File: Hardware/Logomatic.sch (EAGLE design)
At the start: 71 parts, among them J1 USD_CONNECTOR, Q1 12MHz, Q2 32kHz, Q4 TRANSISTOR_PNPSMD, U1 MCP73831, U2 3.3V, U4 LPC213X, X1 USB_MICROB_PLUGCONN-11752

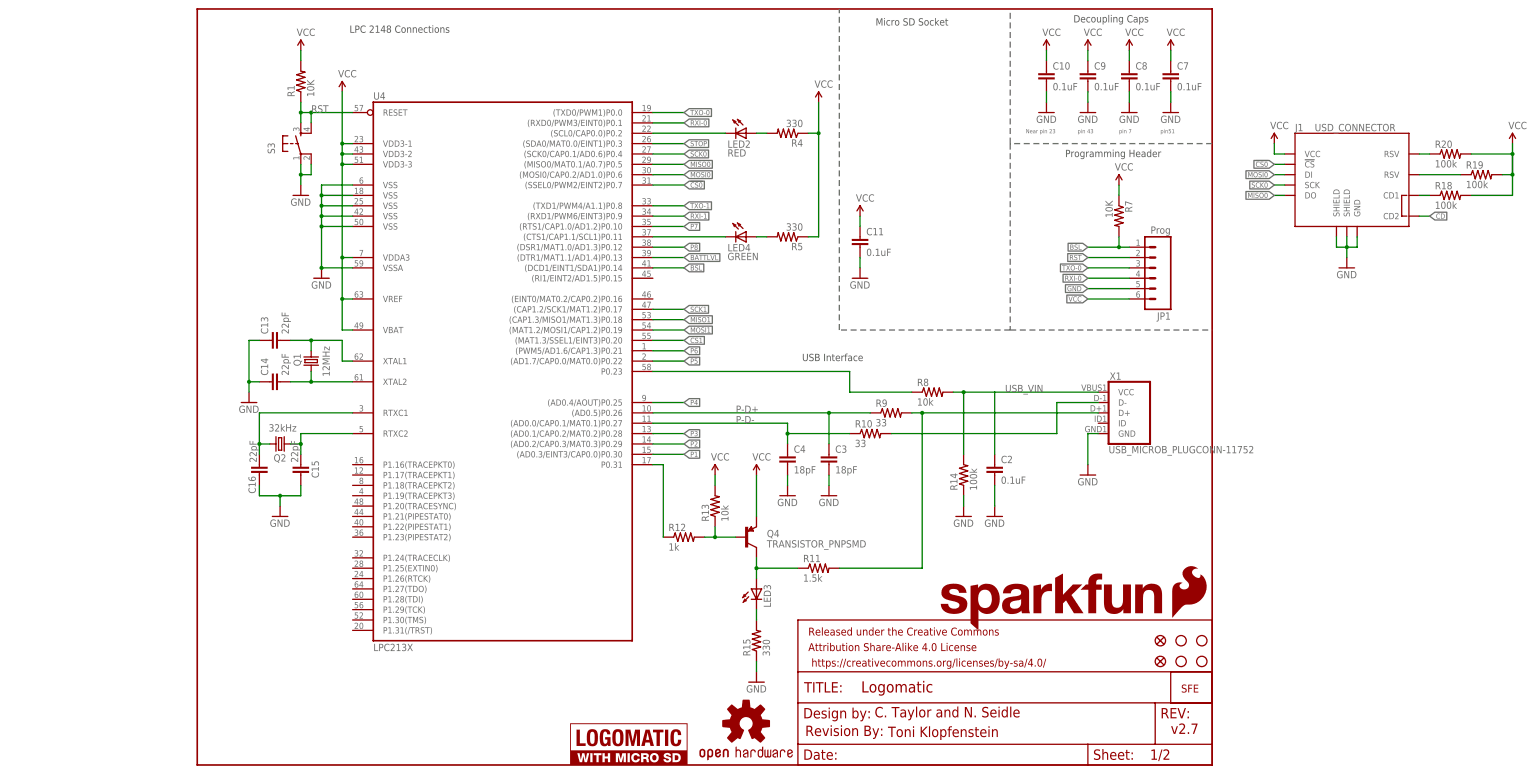
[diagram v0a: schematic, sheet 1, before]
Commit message: Added coin cell holder
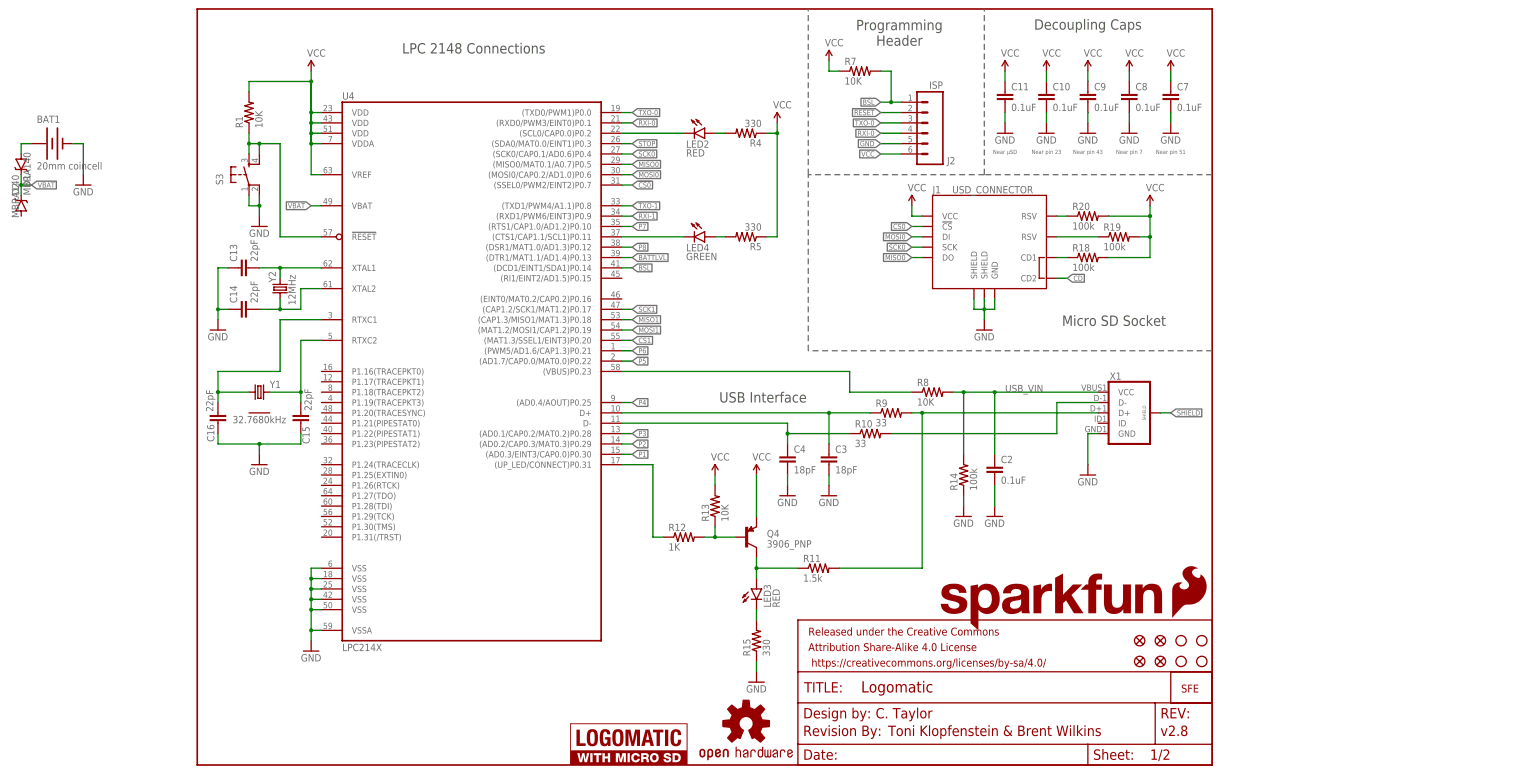
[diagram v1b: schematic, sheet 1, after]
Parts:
- removed JP1: Prog, SparkFun:M06SIP
- removed JP2: LiPo, SparkFun:M02-JST-2MM-SMT
- removed JP4: (no value), SparkFun:M04PTH
- removed JP5: (no value), SparkFun:M06SIP
- removed JP6: M100.1, SparkFun:M10"
- removed Q1: 12MHz, SparkFunEagle-6-6-07:CRYSTAL5X3
- removed Q2: 32kHz, SparkFun:CRYSTAL32-SMD
- removed U$1, U$2: FIDUCIAL1X2, SparkFun:FIDUCIAL1X2
- removed U$3, U$4, U$5, U$8: STAND-OFF, SparkFun:STAND-OFF
- added BAT1: 20mm coincell, SparkFun-Electromechanical:BATTERY20MM_4LEGS
- added D1, D2: MBRA140, SparkFun-DiscreteSemi:MBRA140
- added FD1, FD2, FD3, FD4: FIDUCIAL1X2, SparkFun-Aesthetics:FIDUCIAL1X2
- added H1, H2, H3, H4: STAND-OFF, SparkFun-Electromechanical:STAND-OFF
- added J2: ISP, SparkFun-Connectors:M06SILK_FEMALE_PTH
- added J3: LiPo, SparkFun-Connectors:M02-JST-2MM-SMT
- added J4: (no value), SparkFun-Connectors:M04PTH
- added J5: (no value), SparkFun-Connectors:M06SILK_FEMALE_PTH
- added J6: M100.1, SparkFun-Connectors:M10SILK_FEMALE_PTH
- added Y1: 32.7680kHz, Logomatic_testing:RTC_CRYSTAL32-SMD
- added Y2: 12MHz, SparkFun-FreqCtrl:CRYSTALCRYSTAL-SMD-5X3-12MHZ
- FRAME4: value FRAME-LETTER -> FRAME-LETTERNO_PACKAGE; device SparkFun-Aesthetics:FRAME-LETTER -> SparkFun-Aesthetics:FRAME-LETTERNO_PACKAGE
- LED1: value LED RED -> RED
- LED3: value (none) -> RED
- Q4: value TRANSISTOR_PNPSMD -> 3906_PNP; device SparkFun:TRANSISTOR_PNPSMD -> SparkFun-DiscreteSemi:TRANSISTOR_PNPPMBT3906
- R1, R6, R7: device SparkFun-Resistors:10KOHM1/10W1%(0603)0603 -> SparkFun-Resistors:10KOHM-1/10W-1%(0603)0603
- R12: value 1k -> 1K; device SparkFun-Resistors:1KOHM1/10W1%(0603) -> SparkFun-Resistors:1KOHM-1/10W-1%(0603)
- R13, R8: value 10k -> 10K; device SparkFun-Resistors:10KOHM1/10W1%(0603)0603 -> SparkFun-Resistors:10KOHM-1/10W-1%(0603)0603
- R14: device SparkFun-Resistors:100KOHM1/10W1%(0603) -> SparkFun-Resistors:100KOHM-1/10W-1%(0603)
- R16, R17: value 1M -> DNP; device SparkFun-Resistors:1MOHM1/10W1%(0603) -> SparkFun-Resistors:1MOHM-1/10W-1%(0603)
- S1: device SparkFun:SWITCH-SPSTSMD -> SparkFun-Electromechanical:SWITCH-SPDTSMD
- S2: value Stop -> TAC_SWITCHSMD; device SparkFunEagle-6-6-07:TAC_SWITCHSND -> SparkFun-Retired:TAC_SWITCHSMD
- S3: value Reset -> RESET; device SparkFunEagle-6-6-07:TAC_SWITCHSND -> SparkFun-Retired:TAC_SWITCHSMD
- U1: device SparkFun:MCP73831SMD -> SparkFun-PowerIC:MCP73831
- U2: device SparkFun:V_REG_LDOSMD -> SparkFun-PowerIC:MIC52053.3V
- U4: value LPC213X -> LPC214X; device SparkFun:LPC213X -> SparkFun-DigitalIC:LPC214X
- X1: value USB_MICROB_PLUGCONN-11752 -> (none)
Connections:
- removed net N$16: R8.1, U4.P0.23
- removed net N$21: C14.2, Q1.1, U4.XTAL2
- removed net N$31: R12.1, U4.P0.31
- removed net N$5: C13.2, Q1.2, U4.XTAL1
- removed net N$6: C16.2, Q2.2, U4.RTXC1
- removed net N$9: C15.2, Q2.1, U4.RTXC2
- removed net RST: JP1.2, R1.1, S3.3, S3.4, U4.RESET
- new net !RESET: J2.2, R1.1, S3.3, S3.4, U4.!RESET
- new net N$2: BAT1.+, D1.A
- new net RTXC1: C16.2, U4.RTXC1, Y1.1
- new net RTXC2: C15.2, U4.RTXC2, Y1.4
- new net SHIELD: X1.SHIELD
- new net UP_LED: R12.1, U4.(UP_LED/CONNECT)P0.31
- new net VBAT: D1.C, D2.C, U4.VBAT
- new net VBUS: R8.1, U4.(VBUS)P0.23
- new net XTAL1: C13.2, U4.XTAL1, Y2.2
- new net XTAL2: C14.2, U4.XTAL2, Y2.1
- net BSL: now also J2.1; no longer JP1.1
- net CS1: now also J4.1; no longer JP4.1
- net GND: now also BAT1.-, J2.5, J3.2, J5.4, J6.10, U4.VSS@5; no longer JP1.5, JP2.1, JP5.4, JP6.10, U4.VSS
- net MISO1: now also J4.3; no longer JP4.3
- net MOSI1: now also J4.2; no longer JP4.2
- net P-D+: now also U4.D+; no longer U4.(AD0.5)P0.26
- net P-D-: now also U4.D-; no longer U4.(AD0.0/CAP0.1/MAT0.1)P0.27
- net P1: now also J6.2; no longer JP6.2
- net P2: now also J6.3; no longer JP6.3
- net P3: now also J6.4; no longer JP6.4
- net P4: now also J6.5; no longer JP6.5
- net P5: now also J6.6; no longer JP6.6
- net P6: now also J6.7; no longer JP6.7
- net P7: now also J6.8; no longer JP6.8
- net P8: now also J6.9; no longer JP6.9
- net RAW: now also J5.1; no longer JP5.1
- net RXI-0: now also J2.4; no longer JP1.4
- net RXI-1: now also J5.6; no longer JP5.6
- net SCK1: now also J4.4; no longer JP4.4
- net STOP: now also J6.1; no longer JP6.1
- net TXO-0: now also J2.3; no longer JP1.3
- net TXO-1: now also J5.5; no longer JP5.5
- net USB_VIN: now also J5.2; no longer JP5.2
- net VCC: now also J2.6, J5.3, U4.VDD@1, U4.VDD@2, U4.VDD@3, U4.VDDA; no longer JP1.6, JP5.3, U4.VBAT, U4.VDD3-1, U4.VDD3-2, U4.VDD3-3, U4.VDDA3
- net VLIPO: now also J3.1; no longer JP2.2
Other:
- note added: "C. Taylor"
- note added: "Near pin 43"
- note added: "Near pin 51"
- note added: "Near pin 7"
- note added: "Near µSD"
- note added: "Plated Through Holes"
- note added: "Toni Klopfenstein & Brent Wilkins"
- note added: "v2.8"
- note removed: "Breakouts"
- note removed: "C. Taylor and N. Seidle"
- note removed: "Toni Klopfenstein"
- note removed: "pin 43"
- note removed: "pin 7"
- note removed: "pin51"
- note removed: "v2.7"
- moved on the sheet: C10, C11, C13, C14, C15, C16, C7, C8, C9, J1, R1, R18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

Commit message: Tweaks
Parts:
- removed LOGO3: SFE_LOGO_FLAME.4_INCH, SparkFun-Aesthetics:SFE_LOGO_FLAME.4_INCH
- removed U$10: REVISION, SparkFun-Aesthetics:REVISION
- removed U$7: LOGO-SFESK, SparkFun:LOGO-SFESK
- added LOGO5: SFE_LOGO_FLAME.1_INCH, SparkFun-Aesthetics:SFE_LOGO_FLAME.1_INCH
- R11: value 1.5k -> 1.5KOHM; device SparkFun-Resistors:1.5KOHM1/10W1%(0603) -> SparkFun-Resistors:1.5KOHM-1/10W-1%(0603)
- S1: value (none) -> BATTERY_POWER
- X1: value (none) -> Micro-B
- renumbered U$6 to LOGO4
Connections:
- net VCC: now also D2.A
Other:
- note added: "Charge Circuit (1S)"
- note added: "Limit RAW voltage to 6.5V"
- note added: "RTC Battery Backup"
- note removed: "C. Taylor"
- note removed: "Charge Circuit"
- note removed: "Toni Klopfenstein & Brent Wilkins"
- note removed: "v2.8"
- moved on the sheet: C1, C17, C5, J1, J2, J3, J4, J5, J6, LED1, R1, R18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

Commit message: Fixed issue #9 on GitHub
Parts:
- removed FRAME4: FRAME-LETTERNO_PACKAGE, SparkFun-Aesthetics:FRAME-LETTERNO_PACKAGE
- removed LOGO5: SFE_LOGO_FLAME.1_INCH, SparkFun-Aesthetics:SFE_LOGO_FLAME.1_INCH
- removed U4: LPC214X, SparkFun-DigitalIC:LPC214X
- added FRAME1: FRAME-LETTER, SparkFun-Aesthetics:FRAME-LETTER
- added LOGO100: OSHW-LOGOL, SparkFun-Aesthetics:OSHW-LOGOL
- added U3: 3.3V, SparkFun-PowerIC:MIC52053.3V
- C1: value 0.1uF -> 4.7uF; device SparkFun-Capacitors:0.1UF-25V(+80/-20%)(0603) -> SparkFun-Capacitors:4.7UF-6.3V-10%(0603)0603
- C10: value 0.1uF -> 10uF; device SparkFun-Capacitors:0.1UF-25V(+80/-20%)(0603) -> SparkFun-Capacitors:10UF-16V-10%(TANT)
- C12: value 0.1uF -> 22pF; device SparkFun-Capacitors:0.1UF-25V(+80/-20%)(0603) -> SparkFun-Capacitors:22PF-50V-5%(0603)
- C14, C15: value 22pF -> 0.1uF; device SparkFun-Capacitors:22PF-50V-5%(0603) -> SparkFun-Capacitors:0.1UF-25V(+80/-20%)(0603)
- C16: value 22pF -> 18pF; device SparkFun-Capacitors:22PF-50V-5%(0603) -> SparkFun-Capacitors:18PF-50V-5%(0603)
- C17: value 4.7uF -> 0.1uF; device SparkFun-Capacitors:4.7UF-6.3V-10%(0603)0603 -> SparkFun-Capacitors:0.1UF-25V(+80/-20%)(0603)
- C3: value 18pF -> 0.1uF; device SparkFun-Capacitors:18PF-50V-5%(0603) -> SparkFun-Capacitors:0.1UF-25V(+80/-20%)(0603)
- C4: value 18pF -> 4.7uF; device SparkFun-Capacitors:18PF-50V-5%(0603) -> SparkFun-Capacitors:4.7UF-6.3V-10%(0603)0603
- C5: value 4.7uF -> 22pF; device SparkFun-Capacitors:4.7UF-6.3V-10%(0603)0603 -> SparkFun-Capacitors:22PF-50V-5%(0603)
- C6: value 10uF -> 22pF; device SparkFun-Capacitors:10UF-16V-10%(TANT) -> SparkFun-Capacitors:22PF-50V-5%(0603)
- C9: value 0.1uF -> 18pF; device SparkFun-Capacitors:0.1UF-25V(+80/-20%)(0603) -> SparkFun-Capacitors:18PF-50V-5%(0603)
- FRAME2: value FRAME-LETTER -> FRAME-LETTERNO_PACKAGE; device SparkFun-Aesthetics:FRAME-LETTER -> SparkFun-Aesthetics:FRAME-LETTERNO_PACKAGE
- J1: value USD_CONNECTOR -> ISP; device SparkFun-Connectors:USD_CONNECTOR -> SparkFun-Connectors:M06SILK_FEMALE_PTH
- J2: value ISP -> LiPo; device SparkFun-Connectors:M06SILK_FEMALE_PTH -> SparkFun-Connectors:M02-JST-2MM-SMT
- J3: value LiPo -> USD_CONNECTOR; device SparkFun-Connectors:M02-JST-2MM-SMT -> SparkFun-Connectors:USD_CONNECTOR
- J5: value (none) -> M100.1; device SparkFun-Connectors:M06SILK_FEMALE_PTH -> SparkFun-Connectors:M10SILK_FEMALE_PTH
- J6: value M100.1 -> (none); device SparkFun-Connectors:M10SILK_FEMALE_PTH -> SparkFun-Connectors:M06SILK_FEMALE_PTH
- LED2: value RED -> GREEN; device SparkFun-LED:LED-RED0603 -> SparkFun-LED:LED-GREEN0603
- LED4: value GREEN -> RED; device SparkFun-LED:LED-GREEN0603 -> SparkFun-LED:LED-RED0603
- LOGO1: value OSHW-LOGOL -> SFE_LOGO_NAME.1_INCH; device SparkFun-Aesthetics:OSHW-LOGOL -> SparkFun-Aesthetics:SFE_LOGO_NAME.1_INCH
- LOGO2: value SFE_LOGO_NAME.1_INCH -> SFE_LOGO_FLAME.1_INCH; device SparkFun-Aesthetics:SFE_LOGO_NAME.1_INCH -> SparkFun-Aesthetics:SFE_LOGO_FLAME.1_INCH
- R10: value 33 -> 10K; device SparkFun-Resistors:33OHM1/10W1%(0603) -> SparkFun-Resistors:10KOHM-1/10W-1%(0603)0603
- R11: value 1.5KOHM -> 10K; device SparkFun-Resistors:1.5KOHM-1/10W-1%(0603) -> SparkFun-Resistors:10KOHM-1/10W-1%(0603)0603
- R12: value 1K -> 1.5KOHM; device SparkFun-Resistors:1KOHM-1/10W-1%(0603) -> SparkFun-Resistors:1.5KOHM-1/10W-1%(0603)
- R13: value 10K -> 1K; device SparkFun-Resistors:10KOHM-1/10W-1%(0603)0603 -> SparkFun-Resistors:1KOHM-1/10W-1%(0603)
- R14: value 100k -> 10K; device SparkFun-Resistors:100KOHM-1/10W-1%(0603) -> SparkFun-Resistors:10KOHM-1/10W-1%(0603)0603
- R15: value 330 -> 33; device SparkFun-Resistors:330OHM1/10W1%(0603) -> SparkFun-Resistors:33OHM1/10W1%(0603)
- R16: value DNP -> 33; device SparkFun-Resistors:1MOHM-1/10W-1%(0603) -> SparkFun-Resistors:33OHM1/10W1%(0603)
- R17: value DNP -> 100k; device SparkFun-Resistors:1MOHM-1/10W-1%(0603) -> SparkFun-Resistors:100KOHM-1/10W-1%(0603)
- R2: value 2.0k -> 10K; device SparkFun-Resistors:2.0KOHM1/10W5%(0603) -> SparkFun-Resistors:10KOHM-1/10W-1%(0603)0603
- R5: value 330 -> 2.0k; device SparkFun-Resistors:330OHM1/10W1%(0603) -> SparkFun-Resistors:2.0KOHM1/10W5%(0603)
- R6, R7: value 10K -> DNP; device SparkFun-Resistors:10KOHM-1/10W-1%(0603)0603 -> SparkFun-Resistors:1MOHM-1/10W-1%(0603)
- R8: value 10K -> 330; device SparkFun-Resistors:10KOHM-1/10W-1%(0603)0603 -> SparkFun-Resistors:330OHM1/10W1%(0603)
- R9: value 33 -> 330; device SparkFun-Resistors:33OHM1/10W1%(0603) -> SparkFun-Resistors:330OHM1/10W1%(0603)
- S1: value BATTERY_POWER -> RESET; device SparkFun-Electromechanical:SWITCH-SPDTSMD -> SparkFun-Retired:TAC_SWITCHSMD
- S2: value TAC_SWITCHSMD -> BATTERY_POWER; device SparkFun-Retired:TAC_SWITCHSMD -> SparkFun-Electromechanical:SWITCH-SPDTSMD
- S3: value RESET -> TAC_SWITCHSMD
- U2: value 3.3V -> LPC214X; device SparkFun-PowerIC:MIC52053.3V -> SparkFun-DigitalIC:LPC214X
- Y1: value 32.7680kHz -> 12MHz; device Logomatic_testing:RTC_CRYSTAL32-SMD -> SparkFun-FreqCtrl:CRYSTALCRYSTAL-SMD-5X3-12MHZ
- Y2: value 12MHz -> 32.7680kHz; device SparkFun-FreqCtrl:CRYSTALCRYSTAL-SMD-5X3-12MHZ -> Logomatic_testing:RTC_CRYSTAL32-SMD
- renumbered BAT1 to BAT100, D1 to D101, D2 to D100, FD3 to FD100, FD4 to FD101, LOGO4 to LOGO101, Q4 to Q1, R18 to R101, R19 to R100, R20 to R102
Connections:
- net !CS0: now also J3.!CS, U2.(SSEL0/PWM2/EINT2)P0.7; no longer J1.!CS, U4.(SSEL0/PWM2/EINT2)P0.7
- net !RESET: now also J1.2, S1.3, S1.4, U2.!RESET; no longer J2.2, S3.3, S3.4, U4.!RESET
- net BATTLVL: now also R6.1, R7.2, U2.(DTR1/MAT1.1/AD1.4)P0.13; no longer R16.2, R17.1, U4.(DTR1/MAT1.1/AD1.4)P0.13
- net BSL: now also J1.1, R2.2, U2.(DCD1/EINT1/SDA1)P0.14; no longer J2.1, R7.2, U4.(DCD1/EINT1/SDA1)P0.14
- net CD: now also J3.CD2; no longer J1.CD2
- net CS1: now also U2.(MAT1.3/SSEL1/EINT3)P0.20; no longer U4.(MAT1.3/SSEL1/EINT3)P0.20
- net GND: now also C10.-, C12.1, C14.2, C15.2, C16.2, C5.1, C6.1, J1.5, J2.2, J3.GND, J3.SHIELD@1, J3.SHIELD@3, J5.10, J6.4, R17.1, R5.1, R6.2, R9.1, S1.1, S1.2, U2.VSS@1, U2.VSS@2, U2.VSS@3, U2.VSS@4, U2.VSS@5, U2.VSSA, U3.GND; no longer C10.2, C12.2, C14.1, C15.1, C16.1, C5.2, C6.-, J1.GND, J1.SHIELD@1, J1.SHIELD@3, J2.5, J3.2, J5.4, J6.10, R14.1, R15.1, R17.2, R2.1, S2.1, S3.2, U2.GND, U4.VSS@1, U4.VSS@2, U4.VSS@3, U4.VSS@4, U4.VSS@5, U4.VSSA
- net MISO0: now also J3.DO, U2.(MISO0/MAT0.1/A0.7)P0.5; no longer J1.DO, U4.(MISO0/MAT0.1/A0.7)P0.5
- net MISO1: now also U2.(CAP1.3/MISO1/MAT1.3)P0.18; no longer U4.(CAP1.3/MISO1/MAT1.3)P0.18
- net MOSI0: now also J3.DI, U2.(MOSI0/CAP0.2/AD1.0)P0.6; no longer J1.DI, U4.(MOSI0/CAP0.2/AD1.0)P0.6
- net MOSI1: now also U2.(MAT1.2/MOSI1/CAP1.2)P0.19; no longer U4.(MAT1.2/MOSI1/CAP1.2)P0.19
- net N$1: now also R5.2; no longer R2.2
- net N$10: now also J3.RSV@2; no longer J1.RSV@2
- net N$13: now also R8.1; no longer R3.1
- net N$17: now also R11.1, R13.2; no longer R12.2, R13.1
- net N$19: now also LED2.A, R3.2; no longer LED4.A, R5.2
- net N$3: now also J3.CD1; no longer J1.CD1
- net N$33: now also LED4.C, R9.2; no longer LED3.C, R15.2
- net N$4: now also J3.RSV@1; no longer J1.RSV@1
- net N$7: now also LED3.A; no longer LED2.A
- net P-D+: now also C9.1, R15.1, U2.D+; no longer C3.1, R9.1, U4.D+
- net P-D-: now also C16.1, R16.1, U2.D-; no longer C4.1, R10.1, U4.D-
- net P1: now also J5.2, U2.(AD0.3/EINT3/CAP0.0)P0.30; no longer J6.2, U4.(AD0.3/EINT3/CAP0.0)P0.30
- net P2: now also J5.3, U2.(AD0.2/CAP0.3/MAT0.3)P0.29; no longer J6.3, U4.(AD0.2/CAP0.3/MAT0.3)P0.29
- net P3: now also J5.4, U2.(AD0.1/CAP0.2/MAT0.2)P0.28; no longer J6.4, U4.(AD0.1/CAP0.2/MAT0.2)P0.28
- net P4: now also J5.5, U2.(AD0.4/AOUT)P0.25; no longer J6.5, U4.(AD0.4/AOUT)P0.25
- net P5: now also J5.6, U2.(AD1.7/CAP0.0/MAT0.0)P0.22; no longer J6.6, U4.(AD1.7/CAP0.0/MAT0.0)P0.22
- net P6: now also J5.7, U2.(PWM5/AD1.6/CAP1.3)P0.21; no longer J6.7, U4.(PWM5/AD1.6/CAP1.3)P0.21
- net P7: now also J5.8, U2.(RTS1/CAP1.0/AD1.2)P0.10; no longer J6.8, U4.(RTS1/CAP1.0/AD1.2)P0.10
- net P8: now also J5.9, U2.(DSR1/MAT1.0/AD1.3)P0.12; no longer J6.9, U4.(DSR1/MAT1.0/AD1.3)P0.12
- net RAW: now also J6.1, R7.1, S2.O, U3.EN, U3.IN; no longer J5.1, R16.1, S1.O, U2.EN, U2.IN
- net RTXC1: now also C12.2, U2.RTXC1, Y2.1; no longer C16.2, U4.RTXC1, Y1.1
- net RTXC2: now also C13.2, U2.RTXC2, Y2.4; no longer C15.2, U4.RTXC2, Y1.4
- net RXI-0: now also J1.4, U2.(RXD0/PWM3/EINT0)P0.1; no longer J2.4, U4.(RXD0/PWM3/EINT0)P0.1
- net RXI-1: now also J6.6, U2.(RXD1/PWM6/EINT3)P0.9; no longer J5.6, U4.(RXD1/PWM6/EINT3)P0.9
- net SCK0: now also J3.SCK, U2.(SCK0/CAP0.1/AD0.6)P0.4; no longer J1.SCK, U4.(SCK0/CAP0.1/AD0.6)P0.4
- net SCK1: now also U2.(CAP1.2/SCK1/MAT1.2)P0.17; no longer U4.(CAP1.2/SCK1/MAT1.2)P0.17
- net STAT: now also LED4.A, R12.1; no longer LED3.A, R11.1
- net STAT0: now also LED3.C, U2.(SCL0/CAP0.0)P0.2; no longer LED2.C, U4.(SCL0/CAP0.0)P0.2
- net STAT1: now also LED2.C, U2.(CTS1/CAP1.1/SCL1)P0.11; no longer LED4.C, U4.(CTS1/CAP1.1/SCL1)P0.11
- net STOP: now also C15.1, J5.1, R10.1, S3.3, U2.(SDA0/MAT0.0/EINT1)P0.3; no longer C1.1, J6.1, R6.1, S2.3, U4.(SDA0/MAT0.0/EINT1)P0.3
- net TXO-0: now also J1.3, U2.(TXD0/PWM1)P0.0; no longer J2.3, U4.(TXD0/PWM1)P0.0
- net TXO-1: now also J6.5, U2.(TXD1/PWM4/A1.1)P0.8; no longer J5.5, U4.(TXD1/PWM4/A1.1)P0.8
- net UP_LED: now also R13.1, U2.(UP_LED/CONNECT)P0.31; no longer R12.1, U4.(UP_LED/CONNECT)P0.31
- net USB_D+: now also R12.2, R15.2; no longer R11.2, R9.2
- net USB_D-: now also R16.2; no longer R10.2
- net USB_VIN: now also C1.1, J6.2, R17.2; no longer C2.1, J5.2, R3.2
- net VBAT: now also U2.VBAT; no longer U4.VBAT
- net VBUS: now also R14.1, U2.(VBUS)P0.23; no longer R8.1, U4.(VBUS)P0.23
- net VCC: now also C10.+, C14.1, C2.1, C3.1, J1.6, J3.VCC, J6.3, R10.2, R11.2, R2.1, R3.1, U2.VDD@1, U2.VDD@2, U2.VDD@3, U2.VDDA, U2.VREF, U3.OUT; no longer C10.1, C12.1, C6.+, C9.1, J1.VCC, J2.6, J5.3, R13.2, R5.1, R6.2, R7.1, U2.OUT, U4.VDD@1, U4.VDD@2, U4.VDD@3, U4.VDDA, U4.VREF
- net VLIPO: now also C4.1, J2.1, S2.P; no longer C5.1, J3.1, S1.P
- net XTAL1: now also C6.2, U2.XTAL1, Y1.2; no longer C13.2, U4.XTAL1, Y2.2
- net XTAL2: now also C5.2, U2.XTAL2, Y1.1; no longer C14.2, U4.XTAL2, Y2.1
